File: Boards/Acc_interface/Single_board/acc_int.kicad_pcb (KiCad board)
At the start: 4 copper layers, 85 x 70 mm, 8 parts, among them J1 Ampseal_23_VT, J2 MM_F_RA_20, J3 MM_F_RA_04, J4 MM_F_RA_14, J5 MM_F_RA_06, J6 MicroFit_RA_10, U1 RJ45_VT, U2 RJ45_VT

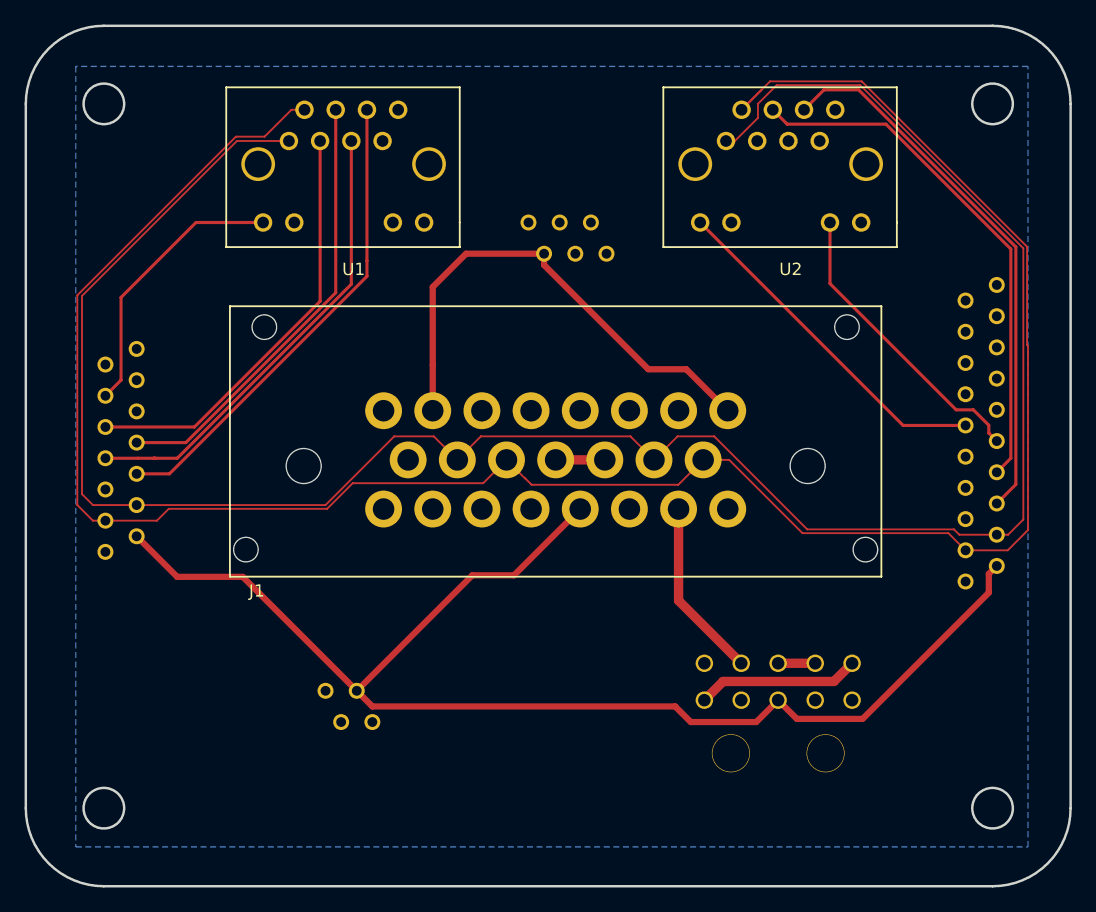
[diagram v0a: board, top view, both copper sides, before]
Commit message: single board acc interface second pass
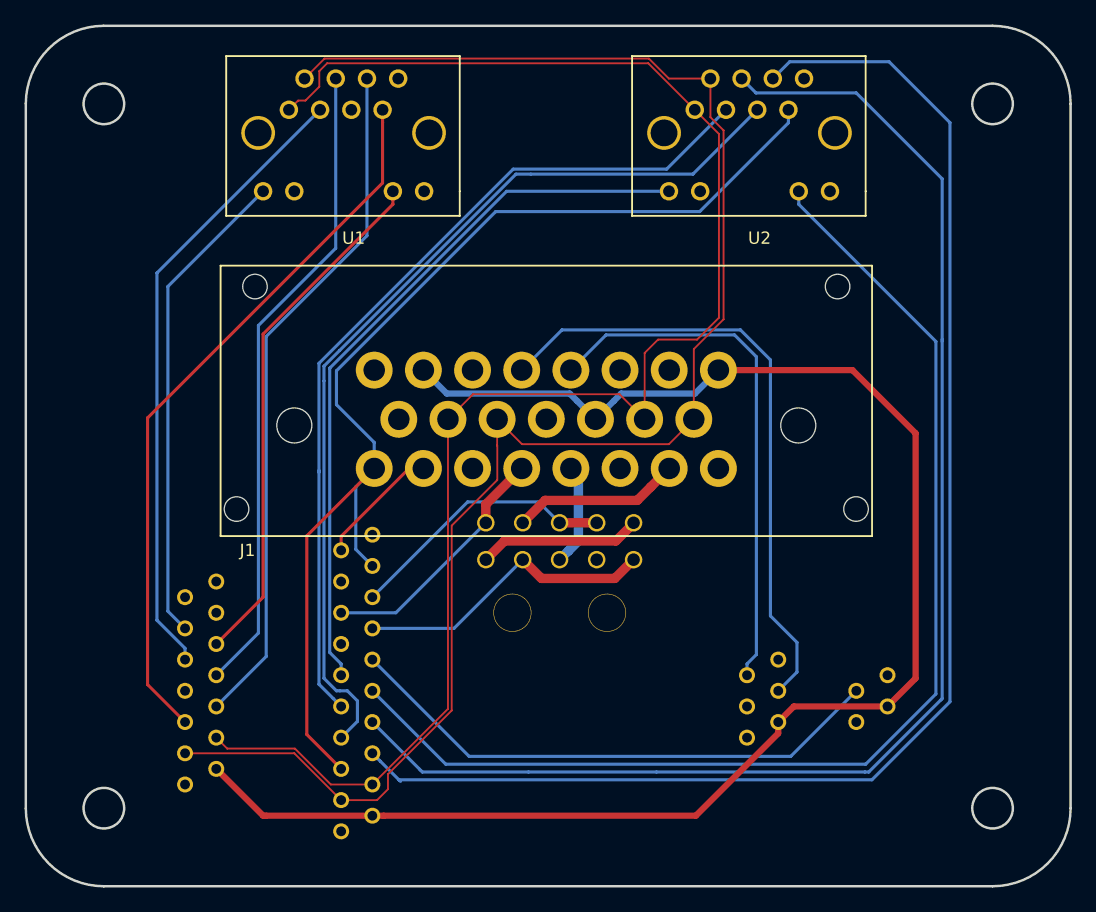
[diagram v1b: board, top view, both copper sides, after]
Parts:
- moved J2 54.7 mm to (134.6, 100.3)
- moved J3 44.7 mm to (176.5, 91.4), turned to 0 degrees
- moved J5 39.0 mm to (167.6, 92.7), turned to 0 degrees
- moved J6 21.1 mm to (152.4, 87.6)
- moved J4 20.0 mm to (121.9, 96.5)
- moved U2 3.59 mm to (161.3, 53.3)
- moved J1 3.39 mm to (130.8, 72.4)
- moved U1 2.54 mm to (128.3, 53.3)
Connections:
- J1 pad 12: /TSMS -> GND
- J1 pad 13: /TSMS -> /12V
- J1 pad 16: /5V_BMS -> /5V_AIR
- J1 pad 19: GND -> /Shutdown_IMD
- J1 pad 20: /12V -> /Shutdown_Final
- J2 pad 18: /5V_BMS -> /5V_AIR
- J6 pad 3: /12V -> /Shutdown_Final
- U1 pad 11: Net-(U1-Pad11) -> GND
- U1 pad 13: Net-(U1-Pad13) -> GND
- U1 pad 14: Net-(U1-Pad14) -> GND
- U1 pad 9: Net-(U1-Pad9) -> GND
- U2 pad 11: Net-(U2-Pad11) -> GND
- U2 pad 13: Net-(U2-Pad13) -> GND
- U2 pad 14: Net-(U2-Pad14) -> GND
- U2 pad 9: Net-(U2-Pad9) -> GND
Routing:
- net /LED1_AIR: track 24.2 -> 96.2 mm
- net /MOSI_AIR: track 44.7 -> 114.8 mm
- net /5V_BMS: track 129.0 -> 59.0 mm
- net /SCK_AIR: track 42.7 -> 112.5 mm
- net /BMS_SENSE: track 78.3 -> 14.8 mm
- net /CAN_HIGH: track 182.3 -> 133.4 mm
- net /CAN_LOW: track 179.3 -> 131.5 mm
- net /12V: track 176.6 -> 129.1 mm
- net /Cooling_pressure_sense: track 57.0 -> 10.1 mm
- net /5V_AIR: track 47.1 -> 92.4 mm
- net /TSAL+_R: track 18.5 -> 59.3 mm
- net /TSAL-_R: track 14.3 -> 51.1 mm
- net /MISO_AIR: track 45.5 -> 76.3 mm
- net /LED2_AIR: track 28.4 -> 58.9 mm
- net /Shutdown_MP: track 54.6 -> 25.8 mm
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- removed copper zone on B.Cu, net GND

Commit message: added ground plane to single board acc interface
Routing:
- added copper zone on In1.Cu, net GND
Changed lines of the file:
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@@
   )
   (setup
-    (last_trace_width 0.254)
+    (last_trace_width 0.1524)
     (user_trace_width 0.1524)
     (user_trace_width 0.254)
@@
   (segment (start 120.523 61.087) (end 128.27 53.34) (width 0.254) (layer B.Cu) (net 33))
   (segment (start 120.523 87.503) (end 120.523 61.087) (width 0.254) (layer B.Cu) (net 33))
+  (zone (net 3) (net_name GND) (layer In1.Cu) (hatch edge 0.508)
+    (connect_pads (clearance 0.508))
+    (min_thickness 0.254)
+    (fill yes (arc_segments 16) (thermal_gap 0.508) (thermal_bridge_width 0.508))
+    (polygon
+      (pts
+        (xy 118.11 41.91) (xy 118.11 107.95) (xy 184.15 107.95) (xy 184.15 41.91)
+      )
+    )
+  )
 )

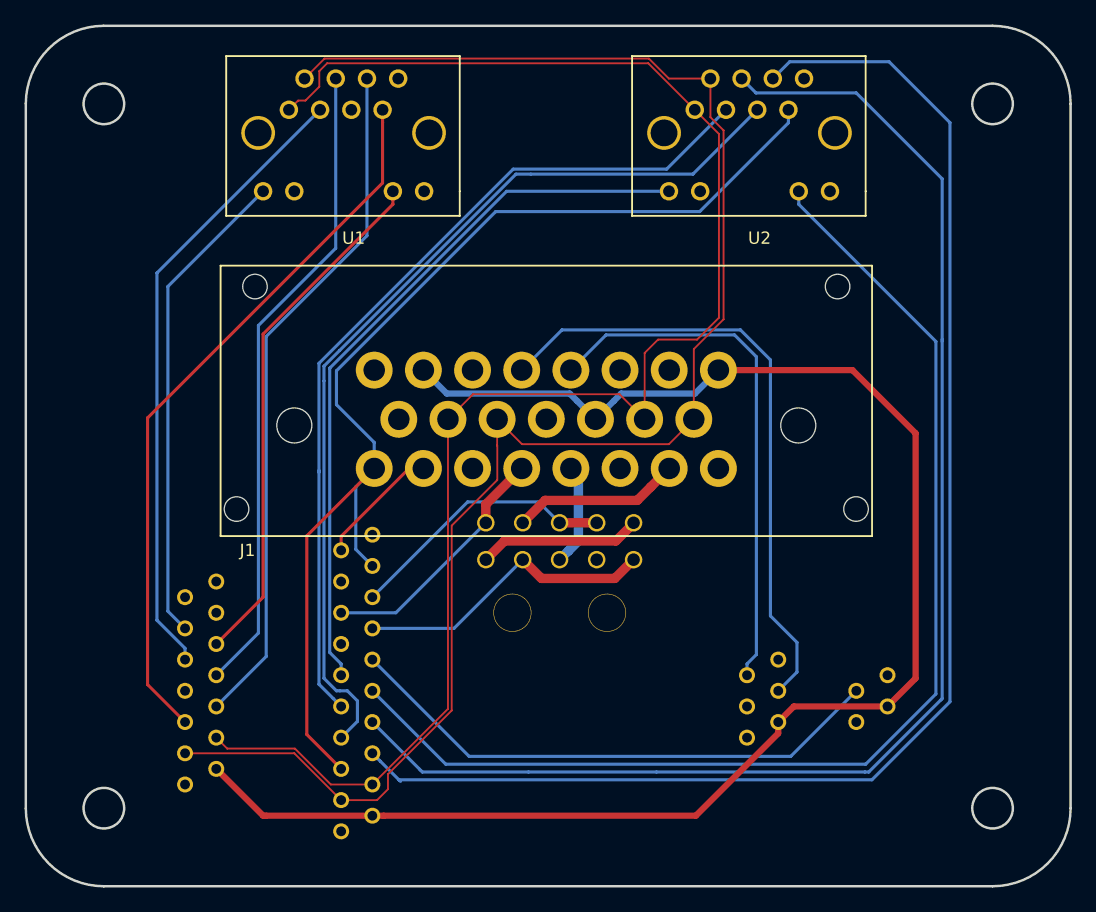
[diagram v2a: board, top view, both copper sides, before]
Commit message: better connector spacing
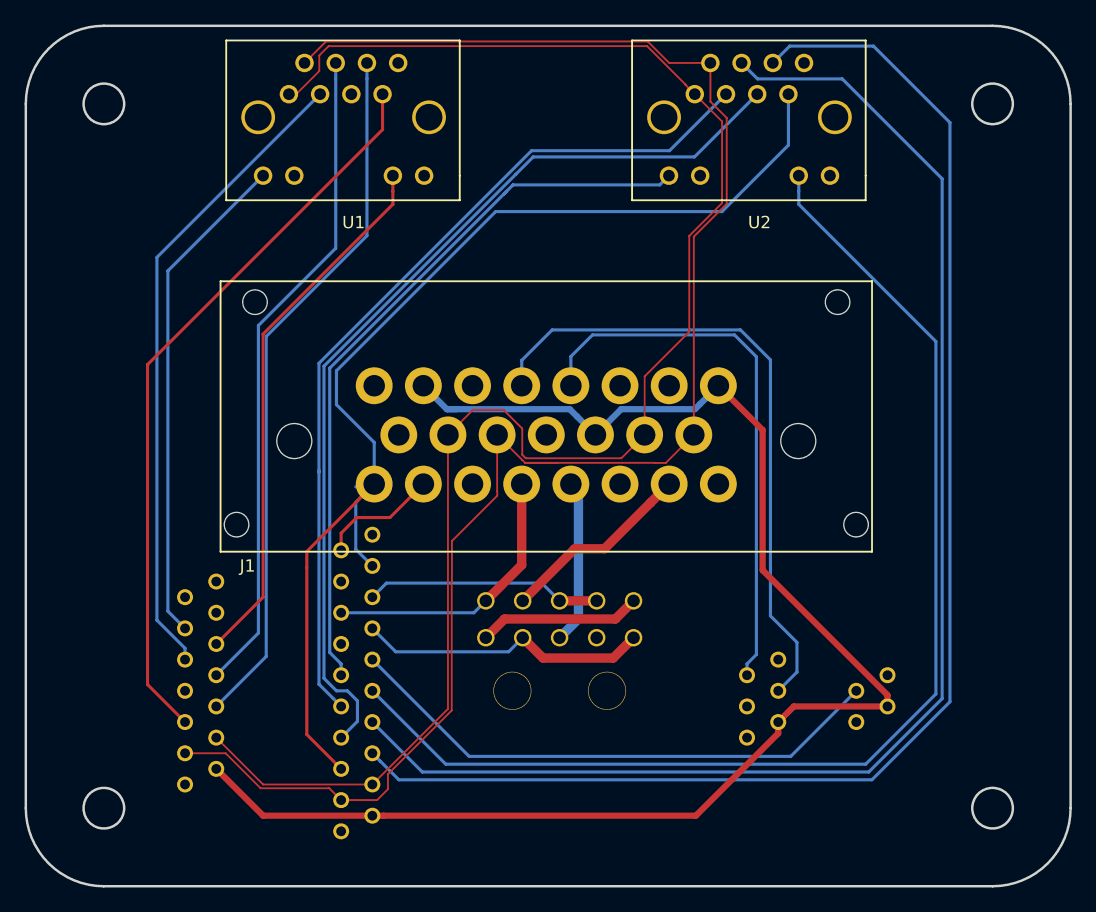
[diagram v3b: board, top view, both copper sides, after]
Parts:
- moved J6 6.35 mm to (152.4, 94.0)
- moved U1 1.27 mm to (128.3, 52.1)
- moved U2 1.27 mm to (161.3, 52.1)
- moved J1 1.27 mm to (130.8, 73.7)
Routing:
- net /12V: track 129.1 -> 120.3 mm
- net /Shutdown_Final: track 8.32 -> 13.4 mm
- net /CAN_HIGH: track 133.4 -> 137.9 mm
- net /5V_AIR: track 92.4 -> 95.6 mm
- net /Shutdown_HVD: track 22.2 -> 19.3 mm
- net /CAN_LOW: track 131.5 -> 134.0 mm
- net /Shutdown_IMD: track 20.4 -> 22.9 mm
- net /Shutdown_E-STOP: track 13.8 -> 15.9 mm
- net /TSAL+_G: track 43.2 -> 45.2 mm
- net /TSAL-_R: track 51.1 -> 52.8 mm
- net /TSAL+_R: track 59.3 -> 60.7 mm
- net /LED1_AIR: track 96.2 -> 97.5 mm
- net /SCK_BMS: track 52.6 -> 53.8 mm
- net /RESET_BMS: track 51.2 -> 52.4 mm
- net /MOSI_BMS: track 56.2 -> 57.4 mm
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
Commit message: added silkscreen to all acc interface boards
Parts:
- added G***: LOGO, footprints:Olin_O, B.Cu at (148.6, 57.1)
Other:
- board text added: "AIR Control"
- board text added: "AIR Prog"
- board text added: "Accumulator Interface Rev 1 Bryce Mann"
- board text added: "BMS Core"
- board text added: "BMS Prog"
- board text added: "IMD Latch"
- board text added: "Shutdown"
- board text added: "TSAL"
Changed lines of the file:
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@@
   (general
     (thickness 1.6)
-    (drawings 14)
+    (drawings 22)
     (tracks 256)
     (zones 0)
-    (modules 8)
+    (modules 9)
     (nets 34)
   )
@@
   )
   (setup
-    (last_trace_width 0.254)
+    (last_trace_width 0.1524)
     (user_trace_width 0.1524)
     (user_trace_width 0.254)
@@
   (module footprints:micromatch_female_ra_20 (layer B.Cu)
     (at 134.62 100.33)
-    (fp_text reference J2 (at 5.08 -5.08) (layer B.SilkS)
+    (fp_text reference J2 (at -1.27 -22.86) (layer B.SilkS)
       (effects (font (size 1 1) (thickness 0.15)) (justify mirror))
     )
@@
   (module footprints:micromatch_female_ra_4 (layer B.Cu)
     (at 176.53 91.44)
-    (fp_text reference J3 (at 5.08 0) (layer B.SilkS)
+    (fp_text reference J3 (at -1.27 -2.54) (layer B.SilkS)
       (effects (font (size 1 1) (thickness 0.15)) (justify mirror))
     )
@@
   (module footprints:micromatch_female_ra_14 (layer B.Cu)
     (at 121.92 96.52)
-    (fp_text reference J4 (at 5.08 -5.08) (layer B.SilkS)
+    (fp_text reference J4 (at -1.27 -15.24) (layer B.SilkS)
       (effects (font (size 1 1) (thickness 0.15)) (justify mirror))
     )
@@
   (module footprints:micromatch_female_ra_6 (layer B.Cu)
     (at 167.64 92.71)
-    (fp_text reference J5 (at 5.08 -5.08) (layer B.SilkS)
+    (fp_text reference J5 (at -1.27 -5.08) (layer B.SilkS)
       (effects (font (size 1 1) (thickness 0.15)) (justify mirror))
     )
@@
   (module footprints:MicroFit_RA_10 (layer B.Cu)
     (at 152.4 93.98)
-    (fp_text reference J6 (at 0.2286 -8.9154) (layer B.SilkS)
+    (fp_text reference J6 (at -8.89 -8.9154) (layer B.SilkS)
       (effects (font (size 1 1) (thickness 0.15)) (justify mirror))
     )
@@
       (net 3 GND))
   )
+  (module footprints:Olin_O (layer B.Cu)
+    (at 148.59 57.15)
+    (fp_text reference G*** (at 10.16 5.08) (layer B.SilkS) hide
+      (effects (font (size 1.524 1.524) (thickness 0.3)) (justify mirror))
+    )
+    (fp_text value LOGO (at 10.16 7.62) (layer B.SilkS) hide
+      (effects (font (size 1.524 1.524) (thickness 0.3)) (justify mirror))
+    )
+    (fp_poly (pts (xy 0.78907 2.933726) (xy 0.297169 2.603291) (xy -0.249654 2.169905) (xy -0.811 1.670573)
+      (xy -1.346471 1.1423) (xy -1.815667 0.622091) (xy -2.036037 0.345931) (xy -2.493304 -0.320664)
+      (xy -2.866143 -0.986545) (xy -3.148527 -1.632052) (xy -3.33443 -2.237523) (xy -3.417825 -2.783297)
+      (xy -3.392687 -3.249711) (xy -3.252989 -3.617104) (xy -3.251451 -3.6195) (xy -3.169272 -3.757194)
+      (xy -3.151881 -3.805837) (xy -3.238357 -3.784085) (xy -3.451232 -3.729169) (xy -3.753084 -3.650766)
+      (xy -3.937 -3.602827) (xy -4.929803 -3.301284) (xy -5.762117 -2.955854) (xy -6.437575 -2.564339)
+      (xy -6.959808 -2.124543) (xy -7.332449 -1.634266) (xy -7.40086 -1.507176) (xy -7.582592 -0.976433)
+      (xy -7.604253 -0.451032) (xy -7.475103 0.063274) (xy -7.204403 0.560731) (xy -6.801416 1.035585)
+      (xy -6.275401 1.482082) (xy -5.63562 1.894469) (xy -4.891334 2.266991) (xy -4.051805 2.593894)
+      (xy -3.126293 2.869426) (xy -2.12406 3.087831) (xy -1.054367 3.243355) (xy 0.073526 3.330246)
+      (xy 0.403482 3.341618) (xy 1.526631 3.369785) (xy 0.78907 2.933726)) (layer B.SilkS) (width 0.01))
+    (fp_poly (pts (xy 3.442983 3.189143) (xy 3.593457 3.149129) (xy 3.859628 3.080824) (xy 4.192829 2.996675)
+      (xy 4.318 2.965353) (xy 4.950523 2.771412) (xy 5.589166 2.511366) (xy 6.187709 2.208074)
+      (xy 6.699928 1.884399) (xy 7.006464 1.635631) (xy 7.427728 1.15255) (xy 7.68721 0.655705)
+      (xy 7.791208 0.151883) (xy 7.746021 -0.352128) (xy 7.557949 -0.849541) (xy 7.23329 -1.333569)
+      (xy 6.778343 -1.797426) (xy 6.199408 -2.234324) (xy 5.502783 -2.637476) (xy 4.694767 -3.000096)
+      (xy 3.78166 -3.315395) (xy 2.769759 -3.576588) (xy 2.037525 -3.718298) (xy 1.579989 -3.791873)
+      (xy 1.263227 -3.832252) (xy 1.062288 -3.841026) (xy 0.952225 -3.819783) (xy 0.916988 -3.789688)
+      (xy 0.858074 -3.735928) (xy 0.847963 -3.779733) (xy 0.766319 -3.839404) (xy 0.537525 -3.878973)
+      (xy 0.3175 -3.891838) (xy -0.049381 -3.903054) (xy -0.420533 -3.915266) (xy -0.613858 -3.922106)
+      (xy -0.848176 -3.919314) (xy -0.993137 -3.895498) (xy -1.016025 -3.876157) (xy -1.081706 -3.846379)
+      (xy -1.164166 -3.861997) (xy -1.171663 -3.848862) (xy -1.054877 -3.771153) (xy -0.838402 -3.644985)
+      (xy -0.801282 -3.624227) (xy -0.008948 -3.11414) (xy 0.773964 -2.467576) (xy 1.356472 -1.894766)
+      (xy 2.033545 -1.129263) (xy 2.578075 -0.383663) (xy 3.016751 0.379744) (xy 3.126149 0.605915)
+      (xy 3.414204 1.311966) (xy 3.572957 1.91735) (xy 3.603305 2.429665) (xy 3.50615 2.856508)
+      (xy 3.413505 3.034819) (xy 3.334494 3.173405) (xy 3.358577 3.208225) (xy 3.442983 3.189143)) (layer B.SilkS) (width 0.01))
+  )
+  (gr_text "IMD Latch" (at 173.99 95.25 90) (layer B.SilkS)
+    (effects (font (size 1.5 1.5) (thickness 0.3)) (justify mirror))
+  )
+  (gr_text TSAL (at 165.1 92.71 90) (layer B.SilkS)
+    (effects (font (size 1.5 1.5) (thickness 0.3)) (justify mirror))
+  )
+  (gr_text Shutdown (at 152.4 100.33) (layer B.SilkS)
+    (effects (font (size 1.5 1.5) (thickness 0.3)) (justify mirror))
+  )
+  (gr_text "AIR Control" (at 132.08 92.71 90) (layer B.SilkS)
+    (effects (font (size 1.5 1.5) (thickness 0.3)) (justify mirror))
+  )
+  (gr_text "BMS Core" (at 119.38 91.44 90) (layer B.SilkS)
+    (effects (font (size 1.5 1.5) (thickness 0.3)) (justify mirror))
+  )
+  (gr_text "Accumulator Interface\nRev 1\nBryce Mann" (at 149.86 48.26) (layer B.SilkS)
+    (effects (font (size 1.5 1.5) (thickness 0.3)) (justify mirror))
+  )
+  (gr_text "AIR Prog" (at 182.88 41.91) (layer F.SilkS)
+    (effects (font (size 1.5 1.5) (thickness 0.3)))
+  )
+  (gr_text "BMS Prog" (at 119.38 41.91) (layer F.SilkS)
+    (effects (font (size 1.5 1.5) (thickness 0.3)))
+  )
   (gr_arc (start 187.616 103.528) (end 187.616 109.878) (angle -90) (layer Edge.Cuts) (width 0.2))
